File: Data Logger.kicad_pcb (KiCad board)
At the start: 2 copper layers, 29 parts, among them J1 CONN_01x04_MALE, J2 CONN_01x09_MALE, J3 CONN_01x04_MALE, J4 CONN_MALE_02X03_ODDEVEN, U1 24LC1025, U2 DS1339U-3+, U3 24LC1025, U4 ATMEGA328P-AU, Y1 32 KHz, Y2 16 MHz

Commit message: update schematics
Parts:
- moved J2 206.4 mm to (53.0, 89.4), turned to 90 degrees
- moved H1 202.8 mm to (45.7, 63.5)
- moved R1 195.4 mm to (52.1, 85.7)
- moved H2 192.4 mm to (45.7, 88.9)
- moved BT1 191.9 mm to (45.8, 72.3)
- moved J4 190.2 mm to (88.9, 68.0)
- moved C1 186.1 mm to (62.7, 65.0)
- moved J3 184.5 mm to (80.0, 89.4), turned to 90 degrees
- moved Y1 183.3 mm to (46.4, 79.4), turned to -90 degrees
- moved R2 183.2 mm to (57.1, 84.6), turned to 180 degrees
- moved J1 180.8 mm to (90.9, 79.4)
- moved U3 177.6 mm to (54.6, 66.0)
- moved U2 177.2 mm to (54.6, 79.4)
- moved D1 172.9 mm to (83.8, 64.8)
- moved C5 170.2 mm to (72.7, 64.8)
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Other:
- board outline added: 50.8 x 30.5 mm

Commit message: update schematics
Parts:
- moved R6 1.93 mm to (84.5, 70.5), turned to 180 degrees
- moved R3 1.80 mm to (80.0, 74.4), turned to 180 degrees
- moved R4 1.69 mm to (80.0, 70.6), turned to 180 degrees
- moved R5 1.28 mm to (84.3, 67.3), turned to 180 degrees
- moved R7 1.22 mm to (80.0, 67.4), turned to 180 degrees
- moved Y2 1.02 mm to (67.8, 82.5)
- moved Y1 0.90 mm to (45.7, 80.0)
- moved C3 0.89 mm to (66.4, 63.2)
- moved R1 0.77 mm to (52.3, 85.0)
- moved BT1 0.74 mm to (45.1, 72.4)
- moved R2 0.67 mm to (56.9, 83.9)
- moved U1 0.64 mm to (54.6, 73.0)
- moved U2 0.64 mm to (54.6, 80.0)
- moved U3 0.64 mm to (54.6, 65.4)
- moved C1 0.52 mm to (62.7, 64.5)
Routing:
- net /SCK: track 0.00 -> 106.2 mm, vias 0 -> 7
- net GND: track 0.00 -> 92.1 mm, vias 0 -> 4
- net /Vcc: track 0.00 -> 86.5 mm
- net /SDA: track 0.00 -> 84.9 mm, vias 0 -> 8
- net Net-(BT1-Pad1): track 0.00 -> 73.2 mm, vias 0 -> 6
- net /D2: track 0.00 -> 36.4 mm, vias 0 -> 1
- net /D3: track 0.00 -> 35.5 mm, vias 0 -> 1
- net /TX: track 0.00 -> 31.8 mm, vias 0 -> 3
- net Net-(C2-Pad1): track 0.00 -> 31.6 mm
- net /RX: track 0.00 -> 29.4 mm, vias 0 -> 1
- net Net-(C3-Pad2): track 0.00 -> 29.2 mm, vias 0 -> 4
- net /MOSI: track 0.00 -> 27.6 mm
- net /RESET: track 0.00 -> 26.5 mm, vias 0 -> 2
- net /D4: track 0.00 -> 25.1 mm, vias 0 -> 1
- net /MISO: track 0.00 -> 23.7 mm, vias 0 -> 2
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
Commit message: Completed Routing
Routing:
- net GND: track 92.1 -> 86.8 mm, vias 4 -> 8
- net /Vcc: track 86.5 -> 84.6 mm
- net Net-(C3-Pad2): track 29.2 -> 31.0 mm
- net Net-(BT1-Pad1): track 73.2 -> 74.8 mm
- net /TX: track 31.8 -> 32.9 mm
- net /RX: track 29.4 -> 28.4 mm
- net /D4: track 25.1 -> 25.9 mm
- net /MOSI: vias 0 -> 2
- added copper zone on F.Cu, net /Vcc
- added copper zone on B.Cu, net GND

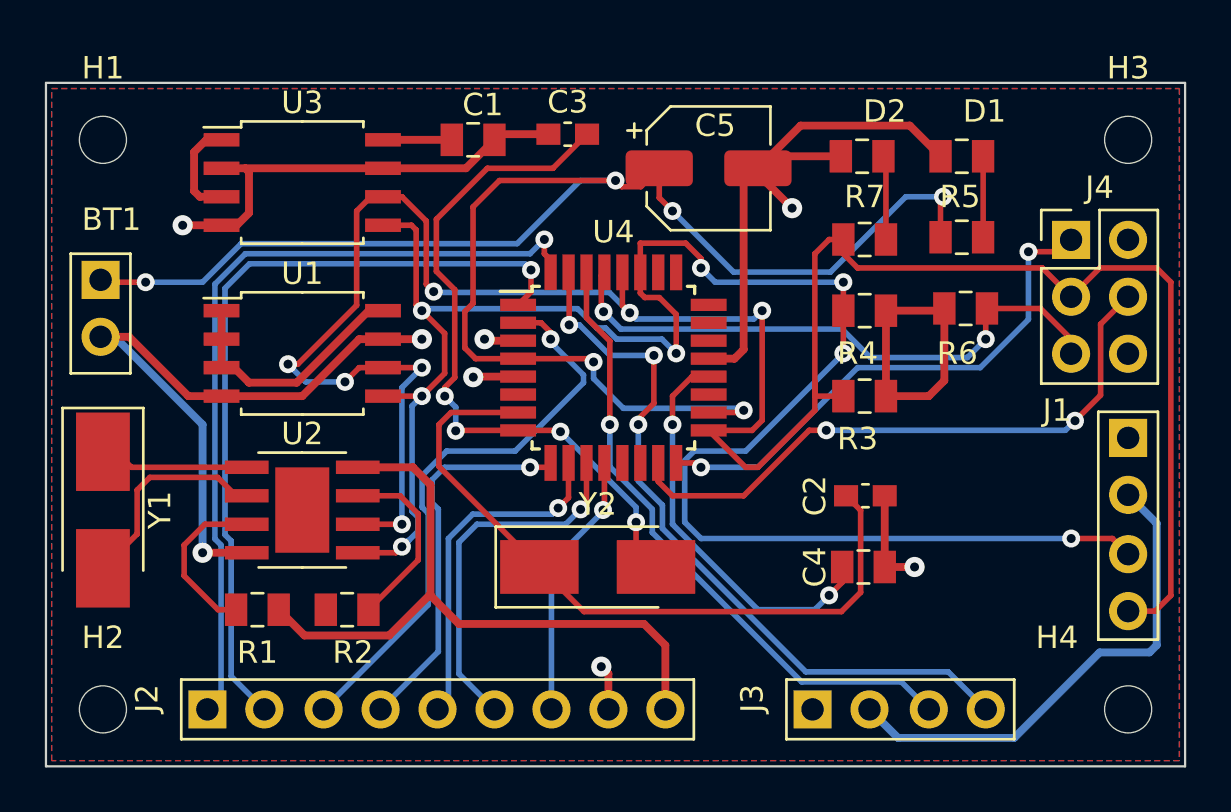
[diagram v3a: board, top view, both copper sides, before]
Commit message: Silkscreen Adjustment
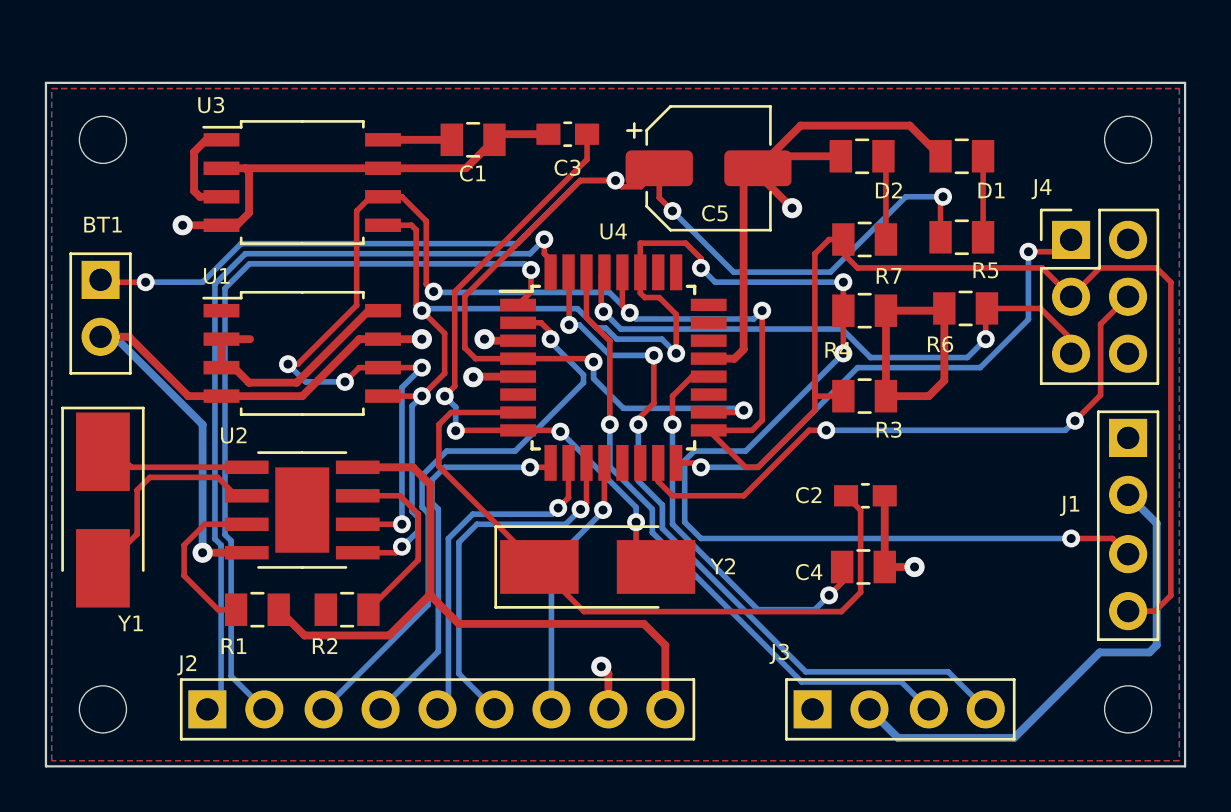
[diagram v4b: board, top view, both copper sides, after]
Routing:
- net Net-(C3-Pad2): track 31.0 -> 28.6 mm
- net Net-(BT1-Pad1): track 74.8 -> 72.7 mm

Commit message: Fixed Routing
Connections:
- BT1 pad 1: Net-(BT1-Pad1) -> /Vcc
- C5 pad 1: Net-(BT1-Pad1) -> /Vcc
- R5 pad 2: Net-(BT1-Pad1) -> /Vcc
- U4 pad 18: Net-(BT1-Pad1) -> /Vcc
- U4 pad 4: Net-(BT1-Pad1) -> /Vcc
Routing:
- net Net-(BT1-Pad1): track 72.7 -> 0.00 mm, vias 6 -> 0
- net /Vcc: track 84.6 -> 156.6 mm, vias 0 -> 6
- net /D2: track 36.4 -> 59.9 mm
- net GND: track 86.8 -> 109.2 mm, vias 8 -> 15
- net /D4: track 25.9 -> 24.7 mm
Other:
- board text added: "GND"
- board text added: "RX"
- board text added: "SCK"
- board text added: "SDA"
- board text added: "TX"
- board text added: "VCC"

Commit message: routing
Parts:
- U2: footprint RN_IC_RTC:U_SMD_DS1339U_DIP08_ANA_DS1339U-3+ -> RN_IC_RTC:U_SMD_DS1339U_TSSOP08_ANA_DS1339U-3+
- moved R1 1.89 mm to (53.2, 83.3), turned to 180 degrees
- moved R7 1.22 mm to (79.2, 68.4), turned to 0 degrees
- moved R2 0.64 mm to (56.9, 83.3)
- moved C5 0.51 mm to (72.7, 64.3)
- moved D1 0.12 mm to (83.9, 64.8)
- moved D2 0.08 mm to (79.2, 64.8)
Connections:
- D2 pad 1: GND -> Net-(D2-Pad1)
- D2 pad 2: Net-(D2-Pad2) -> /SCK
- R7 pad 1: Net-(D2-Pad2) -> GND
- R7 pad 2: /SCK -> Net-(D2-Pad1)
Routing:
- net /Vcc: track 156.6 -> 55.0 mm, vias 6 -> 4
- net GND: track 109.2 -> 43.5 mm, vias 15 -> 12
- net /D2: track 59.9 -> 30.9 mm, vias 1 -> 0
- net /SDA: track 84.4 -> 62.2 mm, vias 8 -> 7
- net /SCK: track 105.9 -> 94.2 mm, vias 7 -> 9
- net /MISO: track 23.7 -> 33.1 mm
- net /D3: track 35.5 -> 26.3 mm, vias 1 -> 0
- net /RX: track 28.4 -> 34.4 mm, vias 1 -> 0
- net /TX: track 32.9 -> 37.8 mm, vias 3 -> 0
- net /D8: track 12.0 -> 16.6 mm, vias 1 -> 0
- net Net-(D2-Pad1): track 0.00 -> 4.32 mm
- net Net-(D2-Pad2): track 3.76 -> 0.00 mm
- net Net-(C3-Pad2): track 28.3 -> 25.2 mm
- net Net-(R1-Pad1): track 7.49 -> 4.47 mm
- net Net-(R2-Pad1): track 8.22 -> 10.3 mm, vias 0 -> 2
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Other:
- copper layers 2 -> 4
